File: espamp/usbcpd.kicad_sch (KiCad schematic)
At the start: 31 parts, among them U301 TPD6S300A, U302 TPS25730D

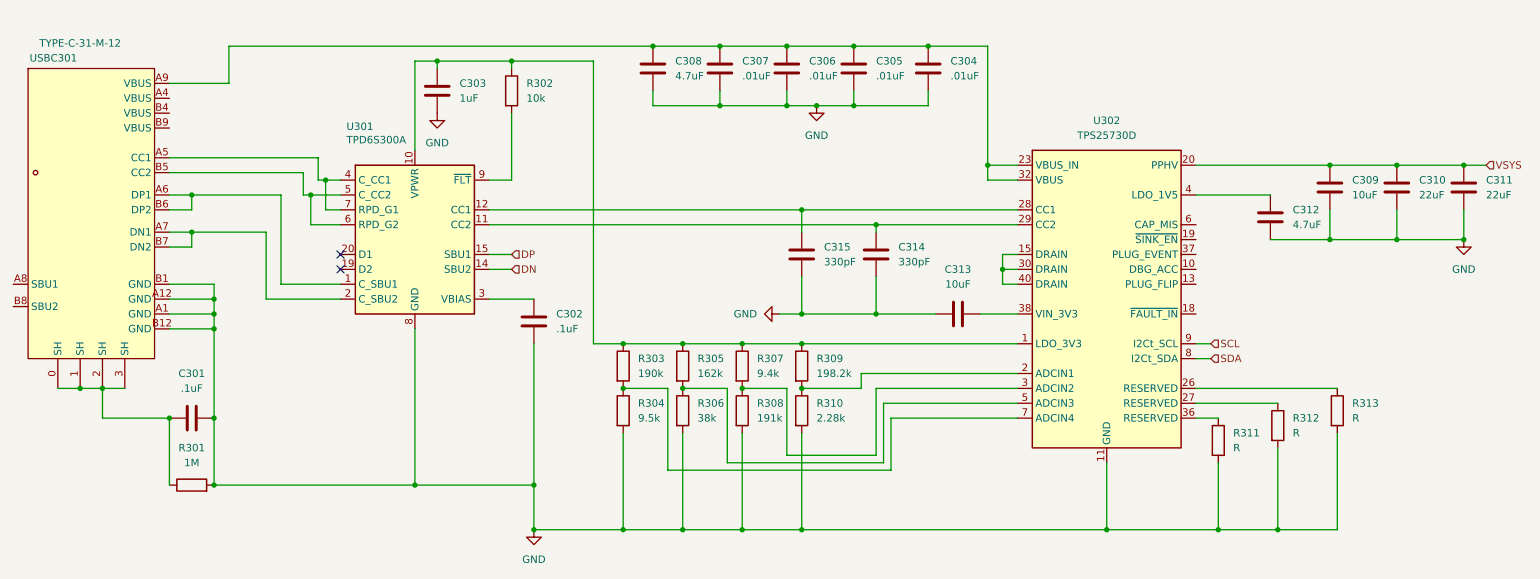
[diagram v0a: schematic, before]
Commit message: setup and route usbc pd
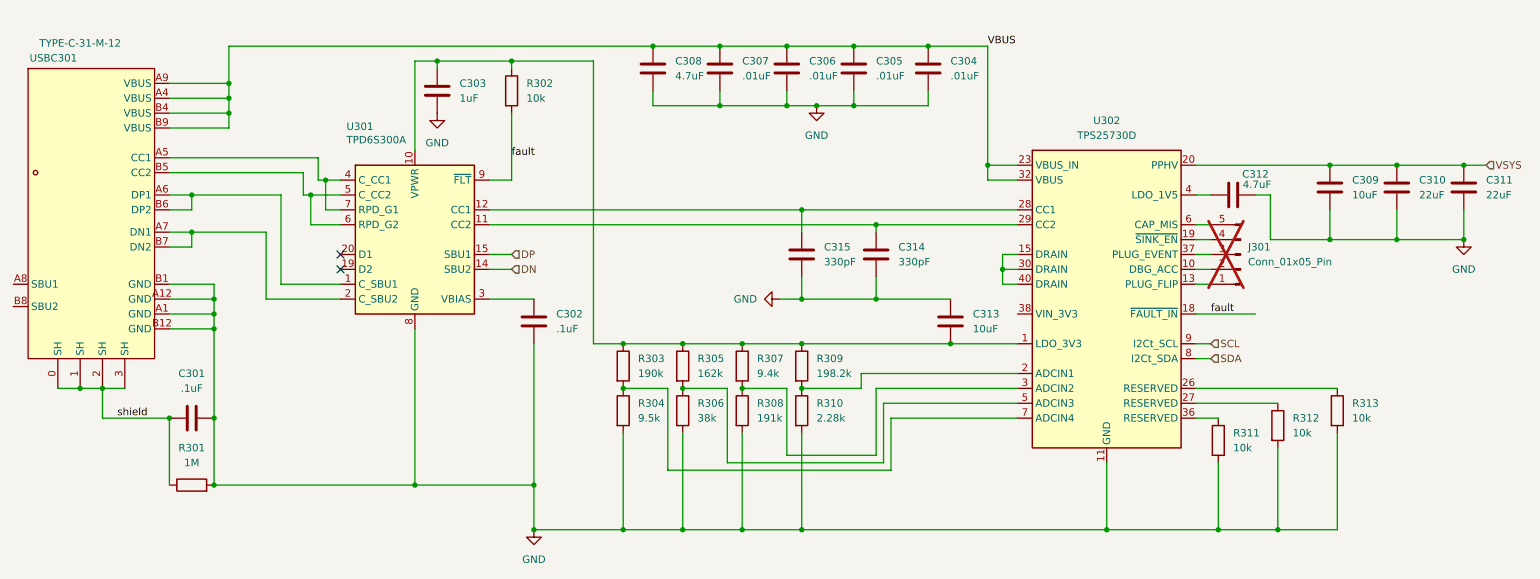
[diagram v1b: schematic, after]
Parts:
- added J301: Conn_01x05_Pin, Connector_PinSocket_1.00mm:PinSocket_1x05_P1.00mm_Vertical, symbol Connector:Conn_01x05_Pin
- C301, C302, C303, C304, C305, C306, C307, C308, C309, C310, C311, C312, C313, C314, C315: footprint (none) -> Capacitor_SMD:C_0603_1608Metric
- R301, R302, R303, R304, R305, R306, R307, R308, R309, R310: footprint (none) -> Resistor_SMD:R_0603_1608Metric
- R311, R312, R313: value R -> 10k; footprint (none) -> Resistor_SMD:R_0603_1608Metric
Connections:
- net GND: now also C313.2; no longer C313.1
- net VBUS: now reaches C304.1, C305.1, C306.1, C307.1, C308.1, U302.23 (VBUS_IN), U302.32 (VBUS), USBC301.A9 (VBUS)
- net VBUS: now also USBC301.A4 (VBUS), USBC301.B4 (VBUS), USBC301.B9 (VBUS)
- net at C303.1, R302.1, R303.1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: now also C313.1
- net fault: now reaches R302.2, U301.9 (~{FLT})
- net fault: now also U302.18 (~{FAULT_IN})
- net at U302.10 (DBG_ACC): now also J301.2 (Pin_2)
- net at U302.13 (PLUG_FLIP): now also J301.1 (Pin_1)
- net at U302.19 (~{SINK_EN}): now also J301.4 (Pin_4)
- net at U302.37 (PLUG_EVENT): now also J301.3 (Pin_3)
- net at U302.38 (VIN_3V3): no longer C313.2
- net at U302.6 (CAP_MIS): now also J301.5 (Pin_5)
- net shield: now reaches C301.1, R301.1, USBC301.0 (SH), USBC301.1 (SH), USBC301.2 (SH), USBC301.3 (SH)
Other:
- moved on the sheet: C312, C313

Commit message: fix config resistors, add test points, increase current handling vias/traces
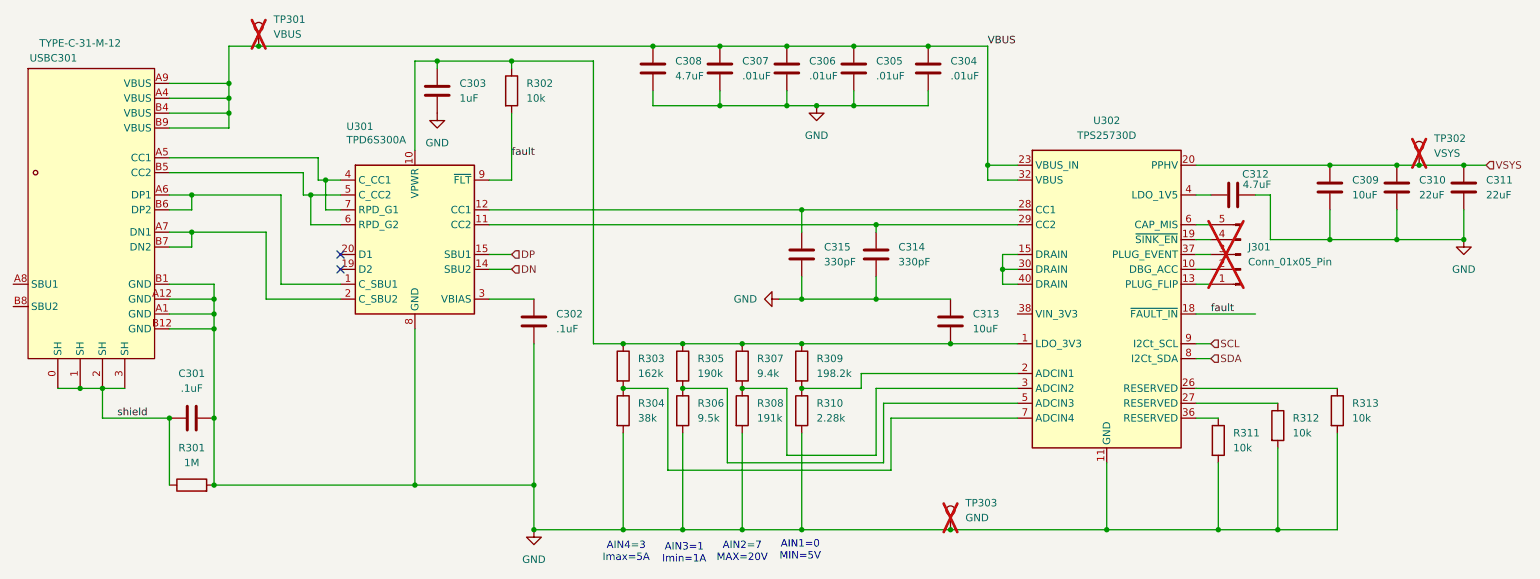
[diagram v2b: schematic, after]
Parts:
- added TP301: VBUS, Connector_Pin:Pin_D1.0mm_L10.0mm, symbol Connector:TestPoint
- added TP302: VSYS, Connector_Pin:Pin_D1.0mm_L10.0mm, symbol Connector:TestPoint
- added TP303: GND, Connector_Pin:Pin_D1.0mm_L10.0mm, symbol Connector:TestPoint
- R303: value 190k -> 162k
- R304: value 9.5k -> 38k
- R305: value 162k -> 190k
- R306: value 38k -> 9.5k
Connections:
- net GND: now also TP303.1
- net VBUS: now also TP301.1
- net VSYS: now also TP302.1
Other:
- note added: "AIN1=0 MIN=5V"
- note added: "AIN2=7 MAX=20V"
- note added: "AIN3=1 Imin=1A"
- note added: "AIN4=3 Imax=5A"

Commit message: Clean up the BOM  - use whole numbers (.1uF -> 100nF)  - capacitor voltage ratings ([22uF](https://jlcpcb.com/partdetail/PANASONIC-EEEFT1H220AR/C336246) at 50V)
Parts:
- removed C304, C305: .01uF, Capacitor_SMD:C_0603_1608Metric, symbol Device:C
- C301, C302: value .1uF -> 100nF
- C306: value .01uF -> 10nF
- C307: value .01uF -> 100nF
- C310, C311: footprint Capacitor_SMD:C_0603_1608Metric -> Capacitor_SMD:C_Elec_5x5.8; symbol Device:C -> Device:C_Polarized
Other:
- moved on the sheet: C306, C307, C308, C309

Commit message: clean up layout
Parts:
- C310, C311: LCSC Part (none) -> C336246
- R304: value 38k -> 37.4
- R305: value 190k -> 191k
- R306: value 9.5k -> 9.31k
- R307: value 9.4k -> 9.31k
- R309: value 198.2k -> 196k
- R310: value 2.28k -> 2.2k
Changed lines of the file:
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@@
 			)
 		)
-		(property "Value" "198.2k"
+		(property "Value" "196k"
 			(at 163.83 107.9499 0)
 			(effects
@@
 			)
 		)
-		(property "Value" "190k"
+		(property "Value" "191k"
 			(at 143.51 107.9499 0)
 			(effects
@@
 			)
 		)
-		(property "Value" "38k"
+		(property "Value" "37.4"
 			(at 133.35 115.5699 0)
 			(effects
@@
 			)
 		)
-		(property "Value" "2.28k"
+		(property "Value" "2.2k"
 			(at 163.83 115.5699 0)
 			(effects
@@
 			)
 		)
+		(property "Label" ""
+			(at 274.32 78.74 0)
+			(effects
+				(font
+					(size 1.27 1.27)
+				)
+				(hide yes)
+			)
+		)
+		(property "LCSC Part" "C336246"
+			(at 274.32 78.74 0)
+			(effects
+				(font
+					(size 1.27 1.27)
+				)
+				(hide yes)
+			)
+		)
 		(pin "1"
 		)
@@
 			)
 		)
-		(property "Value" "9.5k"
+		(property "Value" "9.31k"
 			(at 143.51 115.5699 0)
 			(effects
@@
 			)
 		)
-		(property "Value" "9.4k"
+		(property "Value" "9.31k"
 			(at 153.67 107.9499 0)
 			(effects
@@
 			(at 262.89 78.74 0)
 			(effects
+				(font
+					(size 1.27 1.27)
+				)
+				(hide yes)
+			)
+		)
+		(property "Label" ""
+			(at 262.89 78.74 0)
+			(effects
+				(font
+					(size 1.27 1.27)
+				)
+				(hide yes)
+			)
+		)
+		(property "LCSC Part" "C336246"
+			(at 262.89 78.74 0)
+			(effects

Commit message: amp schematic complete
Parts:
- renumbered C303 to C302, C302 to C303, C308 to C304, C315 to C305, C307 to C306, C314 to C307, C306 to C308, C313 to C309, C312 to C310, C309 to C311, C310 to C312, C311 to C313, TP303 to TP302, TP302 to TP303
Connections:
- net SCL renamed I2C.SCL
- net SDA renamed I2C.SDA
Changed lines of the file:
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@@
 		(at 82.55 87.63)
 	)
+	(bus_entry
+		(at 238.76 100.33)
+		(size -2.54 2.54)
+		(stroke
+			(width 0)
+			(type default)
+		)
+	)
+	(bus_entry
+		(at 238.76 102.87)
+		(size -2.54 2.54)
+		(stroke
+			(width 0)
+			(type default)
+		)
+	)
 	(wire
 		(pts
@@
 	(wire
 		(pts
-			(xy 228.6 102.87) (xy 231.14 102.87)
-		)
-		(stroke
-			(width 0)
-			(type default)
-		)
-	)
-	(wire
-		(pts
 			(xy 148.59 123.19) (xy 148.59 110.49)
 		)
@@
 	(wire
 		(pts
-			(xy 228.6 105.41) (xy 231.14 105.41)
-		)
-		(stroke
-			(width 0)
-			(type default)
-		)
-	)
-	(wire
-		(pts
 			(xy 41.91 115.57) (xy 41.91 110.49)
 		)
@@
 		)
 	)
+	(bus
+		(pts
+			(xy 238.76 100.33) (xy 238.76 102.87)
+		)
+		(stroke
+			(width 0)
+			(type default)
+		)
+	)
 	(wire
 		(pts
@@
 	(wire
 		(pts
+			(xy 228.6 102.87) (xy 236.22 102.87)
+		)
+		(stroke
+			(width 0)
+			(type default)
+		)
+	)
+	(wire
+		(pts
+			(xy 228.6 105.41) (xy 236.22 105.41)
+		)
+		(stroke
+			(width 0)
+			(type default)
+		)
+	)
+	(wire
+		(pts
 			(xy 167.64 59.69) (xy 167.64 62.23)
 		)
@@
 	(label "fault"
 		(at 231.14 97.79 0)
-		(fields_autoplaced yes)
+		(effects
+			(font
+				(size 1.27 1.27)
+			)
+			(justify left bottom)
+		)
+	)
+	(label "I2C.SDA"
+		(at 228.6 105.41 0)
 		(effects
 			(font
@@
 	(label "VBUS"
 		(at 193.04 52.07 0)
-		(fields_autoplaced yes)
 		(effects
 			(font
@@
 		)
 	)
-	(label "shield"
-		(at 44.45 115.57 0)
-		(fields_autoplaced yes)
+	(label "I2C.SCL"
+		(at 228.6 102.87 0)
 		(effects
 			(font
@@
 		)
 	)
-	(label "fault"
-		(at 111.76 71.12 0)
-		(fields_autoplaced yes)
+	(label "shield"
+		(at 44.45 115.57 0)
 		(effects
 			(font
@@
 		)
 	)
-	(hierarchical_label "DN"
-		(shape input)
-		(at 111.76 90.17 0)
-		(fields_autoplaced yes)
+	(label "fault"
+		(at 111.76 71.12 0)
 		(effects
 			(font
 				(size 1.27 1.27)
 			)
-			(justify left)
+			(justify left bottom)
 		)
 	)
-	(hierarchical_label "DP"
+	(hierarchical_label "DN"
 		(shape input)
-		(at 111.76 87.63 0)
-		(fields_autoplaced yes)
+		(at 111.76 90.17 0)
 		(effects
 			(font
@@
 		)
 	)
-	(hierarchical_label "VSYS"
+	(hierarchical_label "I2C{SDA,SCL}"
 		(shape input)
-		(at 278.13 72.39 0)
-		(fields_autoplaced yes)
+		(at 238.76 100.33 0)
 		(effects
 			(font
@@
 		)
 	)
-	(hierarchical_label "SDA"
+	(hierarchical_label "DP"
 		(shape input)
-		(at 231.14 105.41 0)
-		(fields_autoplaced yes)
+		(at 111.76 87.63 0)
 		(effects
 			(font
@@
 		)
 	)
-	(hierarchical_label "SCL"
+	(hierarchical_label "VSYS"
 		(shape input)
-		(at 231.14 102.87 0)
-		(fields_autoplaced yes)
+		(at 278.13 72.39 0)
 		(effects
 			(font
@@
 		(dnp no)
 		(fields_autoplaced yes)
-		(property "Reference" "#PWR0302"
+		(property "Reference" "#PWR0301"
 			(at 99.06 69.85 0)
 			(effects
@@
 			(project "espamp"
 				(path "/48ddfdd8-68fa-4e63-aa18-bc113cdf8cfa/60655049-fbf3-4dfc-8be5-e92116ff6bf0"
-					(reference "#PWR0302")
+					(reference "#PWR0301")
 					(unit 1)
 				)
@@
 		(dnp no)
 		(fields_autoplaced yes)
-		(property "Reference" "#PWR0304"
+		(property "Reference" "#PWR0303"
 			(at 151.13 95.25 0)
 			(effects
@@
 			(project ""
 				(path "/48ddfdd8-68fa-4e63-aa18-bc113cdf8cfa/60655049-fbf3-4dfc-8be5-e92116ff6bf0"
-					(reference "#PWR0304")
+					(reference "#PWR0303")
 					(unit 1)
 				)
@@
 		(dnp no)
 		(fields_autoplaced yes)
-		(property "Reference" "C308"
+		(property "Reference" "C304"
 			(at 158.75 54.6099 0)
 			(effects
@@
 			(project ""
 				(path "/48ddfdd8-68fa-4e63-aa18-bc113cdf8cfa/60655049-fbf3-4dfc-8be5-e92116ff6bf0"
-					(reference "C308")
+					(reference "C304")
 					(unit 1)
 				)
@@
 		(on_board yes)
 		(dnp no)
-		(property "Reference" "C312"
+		(property "Reference" "C310"
 			(at 238.76 73.914 90)
 			(effects
@@
 			(project ""
 				(path "/48ddfdd8-68fa-4e63-aa18-bc113cdf8cfa/60655049-fbf3-4dfc-8be5-e92116ff6bf0"
-					(reference "C312")
+					(reference "C310")
 					(unit 1)
 				)
@@
 		(dnp no)
 		(fields_autoplaced yes)
-		(property "Reference" "C303"
+		(property "Reference" "C302"
 			(at 102.87 58.4199 0)
 			(effects
@@
 			(project ""
 				(path "/48ddfdd8-68fa-4e63-aa18-bc113cdf8cfa/60655049-fbf3-4dfc-8be5-e92116ff6bf0"
-					(reference "C303")
+					(reference "C302")
 					(unit 1)
 				)
@@
 		(dnp no)
 		(fields_autoplaced yes)
-		(property "Reference" "C302"
+		(property "Reference" "C303"
 			(at 119.38 97.7899 0)
 			(effects
@@
 			(project ""
 				(path "/48ddfdd8-68fa-4e63-aa18-bc113cdf8cfa/60655049-fbf3-4dfc-8be5-e92116ff6bf0"
-					(reference "C302")
+					(reference "C303")
 					(unit 1)
 				)
@@
 		(dnp no)
 		(fields_autoplaced yes)
-		(property "Reference" "#PWR0301"
+		(property "Reference" "#PWR0302"
 			(at 115.57 140.97 0)
 			(effects
@@
 			(project ""
 				(path "/48ddfdd8-68fa-4e63-aa18-bc113cdf8cfa/60655049-fbf3-4dfc-8be5-e92116ff6bf0"
-					(reference "#PWR0301")
+					(reference "#PWR0302")
 					(unit 1)
 				)
@@
 		(dnp no)
 		(fields_autoplaced yes)
-		(property "Reference" "C313"
+		(property "Reference" "C309"
 			(at 190.5 97.7899 0)
 			(effects
@@
 			(project "espamp"
 				(path "/48ddfdd8-68fa-4e63-aa18-bc113cdf8cfa/60655049-fbf3-4dfc-8be5-e92116ff6bf0"
-					(reference "C313")
+					(reference "C309")
 					(unit 1)
 				)
@@
 		(dnp no)
 		(fields_autoplaced yes)
-		(property "Reference" "C309"
+		(property "Reference" "C311"
 			(at 255.27 77.4699 0)
 			(effects
@@
 			(project ""
 				(path "/48ddfdd8-68fa-4e63-aa18-bc113cdf8cfa/60655049-fbf3-4dfc-8be5-e92116ff6bf0"
-					(reference "C309")
+					(reference "C311")
 					(unit 1)
 				)
@@
 		(dnp no)
 		(fields_autoplaced yes)
-		(property "Reference" "#PWR0303"
+		(property "Reference" "#PWR0305"
 			(at 274.32 91.44 0)
 			(effects
@@
 			(project ""
 				(path "/48ddfdd8-68fa-4e63-aa18-bc113cdf8cfa/60655049-fbf3-4dfc-8be5-e92116ff6bf0"
-					(reference "#PWR0303")
+					(reference "#PWR0305")
 					(unit 1)
 				)
@@
 		(dnp no)
 		(fields_autoplaced yes)
-		(property "Reference" "C311"
+		(property "Reference" "C313"
 			(at 278.13 76.5809 0)
 			(effects
@@
 			(project "espamp"
 				(path "/48ddfdd8-68fa-4e63-aa18-bc113cdf8cfa/60655049-fbf3-4dfc-8be5-e92116ff6bf0"
-					(reference "C311")
+					(reference "C313")
 					(unit 1)
 				)
@@
 		(dnp no)
 		(fields_autoplaced yes)
-		(property "Reference" "#PWR0305"
+		(property "Reference" "#PWR0304"
 			(at 185.42 68.58 0)
 			(effects
@@
 			(project ""
 				(path "/48ddfdd8-68fa-4e63-aa18-bc113cdf8cfa/60655049-fbf3-4dfc-8be5-e92116ff6bf0"
-					(reference "#PWR0305")
+					(reference "#PWR0304")
 					(unit 1)
 				)
@@
 		(dnp no)
 		(fields_autoplaced yes)
-		(property "Reference" "C315"
+		(property "Reference" "C305"
 			(at 165.1 86.3599 0)
 			(effects
@@
 			(project ""
 				(path "/48ddfdd8-68fa-4e63-aa18-bc113cdf8cfa/60655049-fbf3-4dfc-8be5-e92116ff6bf0"
-					(reference "C315")
+					(reference "C305")
 					(unit 1)
 				)
@@
 		(dnp no)
 		(fields_autoplaced yes)
-		(property "Reference" "C307"
+		(property "Reference" "C306"
 			(at 171.45 54.6099 0)
 			(effects
@@
 			(project ""
 				(path "/48ddfdd8-68fa-4e63-aa18-bc113cdf8cfa/60655049-fbf3-4dfc-8be5-e92116ff6bf0"
-					(reference "C307")
+					(reference "C306")
 					(unit 1)
 				)
@@
 		(dnp no)
 		(fields_autoplaced yes)
-		(property "Reference" "C310"
+		(property "Reference" "C312"
 			(at 266.7 76.5809 0)
 			(effects
@@
 			(project "espamp"
 				(path "/48ddfdd8-68fa-4e63-aa18-bc113cdf8cfa/60655049-fbf3-4dfc-8be5-e92116ff6bf0"
-					(reference "C310")
+					(reference "C312")
 					(unit 1)
 				)
@@
 		(dnp yes)
 		(fields_autoplaced yes)
-		(property "Reference" "TP303"
+		(property "Reference" "TP302"
 			(at 189.23 130.0479 0)
 			(effects
@@
 			(project "espamp"
 				(path "/48ddfdd8-68fa-4e63-aa18-bc113cdf8cfa/60655049-fbf3-4dfc-8be5-e92116ff6bf0"
-					(reference "TP303")
+					(reference "TP302")
 					(unit 1)
 				)
@@
 		(dnp no)
 		(fields_autoplaced yes)
-		(property "Reference" "C306"
+		(property "Reference" "C308"
 			(at 184.15 54.6099 0)
 			(effects
@@
 			(project ""
 				(path "/48ddfdd8-68fa-4e63-aa18-bc113cdf8cfa/60655049-fbf3-4dfc-8be5-e92116ff6bf0"
-					(reference "C306")
+					(reference "C308")
 					(unit 1)
 				)
@@
 		(dnp no)
 		(fields_autoplaced yes)
-		(property "Reference" "C314"
+		(property "Reference" "C307"
 			(at 177.8 86.3599 0)
 			(effects
@@
 			(project ""
 				(path "/48ddfdd8-68fa-4e63-aa18-bc113cdf8cfa/60655049-fbf3-4dfc-8be5-e92116ff6bf0"
-					(reference "C314")
+					(reference "C307")
 					(unit 1)
 				)
@@
 		(dnp yes)
 		(fields_autoplaced yes)
-		(property "Reference" "TP302"
+		(property "Reference" "TP303"
 			(at 269.24 67.8179 0)
 			(effects
@@
 			(project "espamp"
 				(path "/48ddfdd8-68fa-4e63-aa18-bc113cdf8cfa/60655049-fbf3-4dfc-8be5-e92116ff6bf0"
-					(reference "TP302")
+					(reference "TP303")
 					(unit 1)
 				)

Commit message: espamp revisions
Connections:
- net DN renamed USB.DN
- net DP renamed USB.DP
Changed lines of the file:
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@@
+	)
+	(bus_entry
+		(at 116.84 87.63)
+		(size -2.54 2.54)
+		(stroke
+			(width 0)
+			(type default)
+		)
 	)
 	(bus_entry
@@
 		)
 	)
+	(bus_entry
+		(at 116.84 85.09)
+		(size -2.54 2.54)
+		(stroke
+			(width 0)
+			(type default)
+		)
+	)
 	(wire
 		(pts
@@
 	(wire
 		(pts
-			(xy 125.73 102.87) (xy 125.73 54.61)
-		)
-		(stroke
-			(width 0)
-			(type default)
-		)
-	)
-	(wire
-		(pts
 			(xy 180.34 59.69) (xy 180.34 62.23)
 		)
@@
 	(wire
 		(pts
-			(xy 130.81 102.87) (xy 125.73 102.87)
-		)
-		(stroke
-			(width 0)
-			(type default)
-		)
-	)
-	(wire
-		(pts
 			(xy 161.29 91.44) (xy 161.29 95.25)
 		)
@@
 	(wire
 		(pts
-			(xy 111.76 54.61) (xy 125.73 54.61)
+			(xy 111.76 54.61) (xy 130.81 54.61)
 		)
 		(stroke
@@
 	(wire
 		(pts
+			(xy 130.81 54.61) (xy 130.81 102.87)
+		)
+		(stroke
+			(width 0)
+			(type default)
+		)
+	)
+	(wire
+		(pts
 			(xy 154.94 62.23) (xy 167.64 62.23)
 		)
@@
 		)
 	)
+	(bus
+		(pts
+			(xy 116.84 85.09) (xy 116.84 87.63)
+		)
+		(stroke
+			(width 0)
+			(type default)
+		)
+	)
 	(wire
 		(pts
@@
 	(wire
 		(pts
-			(xy 107.95 87.63) (xy 111.76 87.63)
-		)
-		(stroke
-			(width 0)
-			(type default)
-		)
-	)
-	(wire
-		(pts
 			(xy 107.95 82.55) (xy 173.99 82.55)
 		)
@@
 	(wire
 		(pts
+			(xy 107.95 90.17) (xy 114.3 90.17)
+		)
+		(stroke
+			(width 0)
+			(type default)
+		)
+	)
+	(wire
+		(pts
 			(xy 228.6 115.57) (xy 232.41 115.57)
 		)
@@
 	(wire
 		(pts
+			(xy 107.95 87.63) (xy 114.3 87.63)
+		)
+		(stroke
+			(width 0)
+			(type default)
+		)
+	)
+	(wire
+		(pts
 			(xy 161.29 102.87) (xy 186.69 102.87)
 		)
@@
 		(pts
 			(xy 60.96 100.33) (xy 60.96 115.57)
-		)
-		(stroke
-			(width 0)
-			(type default)
-		)
-	)
-	(wire
-		(pts
-			(xy 107.95 90.17) (xy 111.76 90.17)
 		)
 		(stroke
@@
 	(label "fault"
 		(at 231.14 97.79 0)
+		(fields_autoplaced yes)
 		(effects
 			(font
@@
 	(label "I2C.SDA"
 		(at 228.6 105.41 0)
+		(fields_autoplaced yes)
 		(effects
 			(font
@@
 	(label "VBUS"
 		(at 193.04 52.07 0)
+		(fields_autoplaced yes)
 		(effects
 			(font
@@
 	(label "I2C.SCL"
 		(at 228.6 102.87 0)
+		(fields_autoplaced yes)
 		(effects
 			(font
@@
 		)
 	)
-	(label "shield"
-		(at 44.45 115.57 0)
+	(label "USB.DP"
+		(at 107.95 87.63 0)
 		(effects
 			(font
@@
 		)
 	)
-	(label "fault"
-		(at 111.76 71.12 0)
+	(label "shield"
+		(at 44.45 115.57 0)
+		(fields_autoplaced yes)
 		(effects
 			(font
@@
 		)
 	)
-	(hierarchical_label "DN"
+	(label "USB.DN"
+		(at 107.95 90.17 0)
+		(effects
+			(font
+				(size 1.27 1.27)
+			)
+			(justify left bottom)
+		)
+	)
+	(label "fault"
+		(at 111.76 71.12 0)
+		(fields_autoplaced yes)
+		(effects
+			(font
+				(size 1.27 1.27)
+			)
+			(justify left bottom)
+		)
+	)
+	(hierarchical_label "I2C{SDA,SCL}"
 		(shape input)
-		(at 111.76 90.17 0)
+		(at 238.76 100.33 0)
+		(fields_autoplaced yes)
 		(effects
 			(font
@@
 		)
 	)
-	(hierarchical_label "I2C{SDA,SCL}"
+	(hierarchical_label "VSYS"
 		(shape input)
-		(at 238.76 100.33 0)
+		(at 278.13 72.39 0)
+		(fields_autoplaced yes)
 		(effects
 			(font
@@
 		)
 	)
-	(hierarchical_label "DP"
+	(hierarchical_label "USB{DP,DN}"
 		(shape input)
-		(at 111.76 87.63 0)
+		(at 116.84 85.09 0)
+		(fields_autoplaced yes)
 		(effects
 			(font
-				(size 1.27 1.27)
-			)
-			(justify left)
-		)
-	)
-	(hierarchical_label "VSYS"
-		(shape input)
-		(at 278.13 72.39 0)
-		(effects
-			(font
